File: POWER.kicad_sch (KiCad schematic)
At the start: 15 parts, among them U1 XL1509-5.0, U3 SY8089AAC

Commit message: 更新原理图
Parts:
- added C39: 1nF, symbol Device:C_Small
- added D4: SMBJ24A, kicad_api_lib:SMBJ24A, symbol SMBJ24A:D_Schottky_Filled
- added R10: 1M, symbol Device:R_US
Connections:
- net GND: now also C39.1, R10.1
- net VIN: no longer names the net of C2.1, U1.1 (VIN)
- net VIN: now also D4.1 (K)
- new net +24V: D4.2 (A)
- new net Earth: C39.2, R10.2

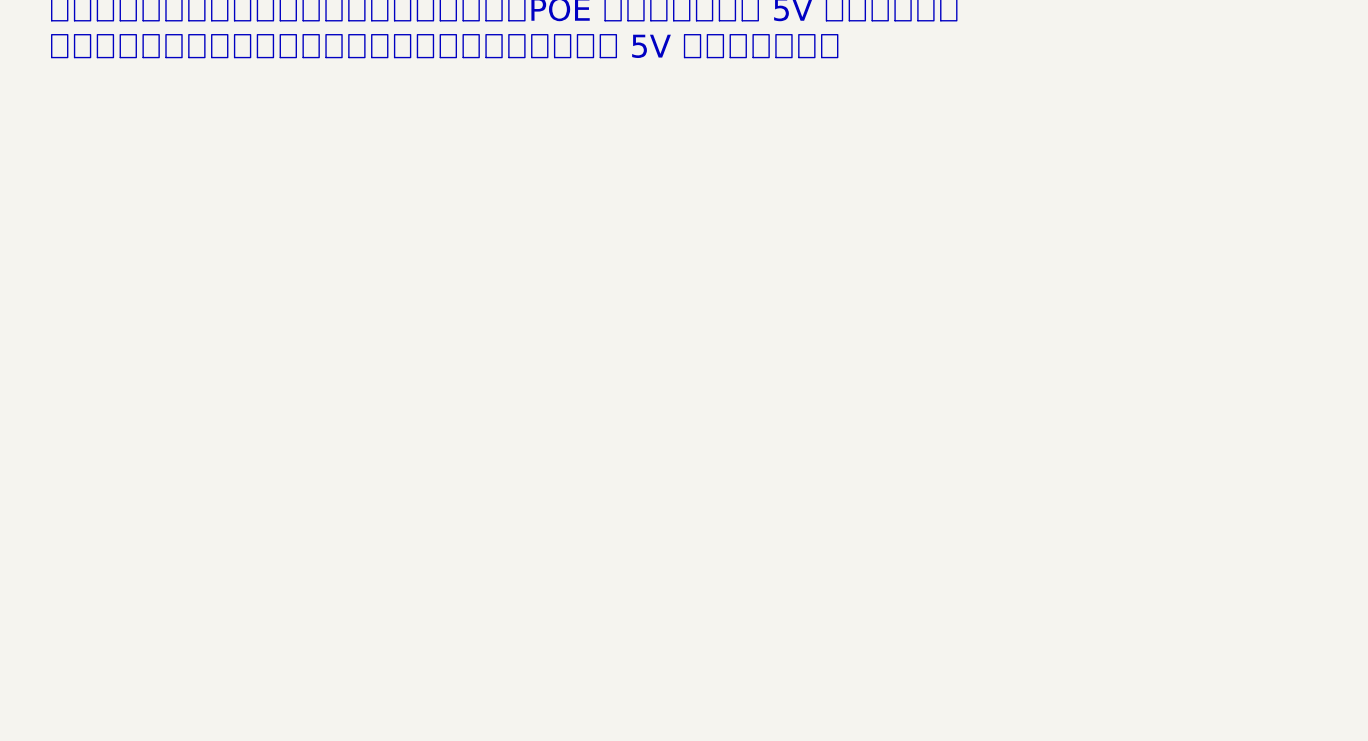
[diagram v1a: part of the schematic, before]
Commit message: 增加USB,TYPEC转串口esd隔离，
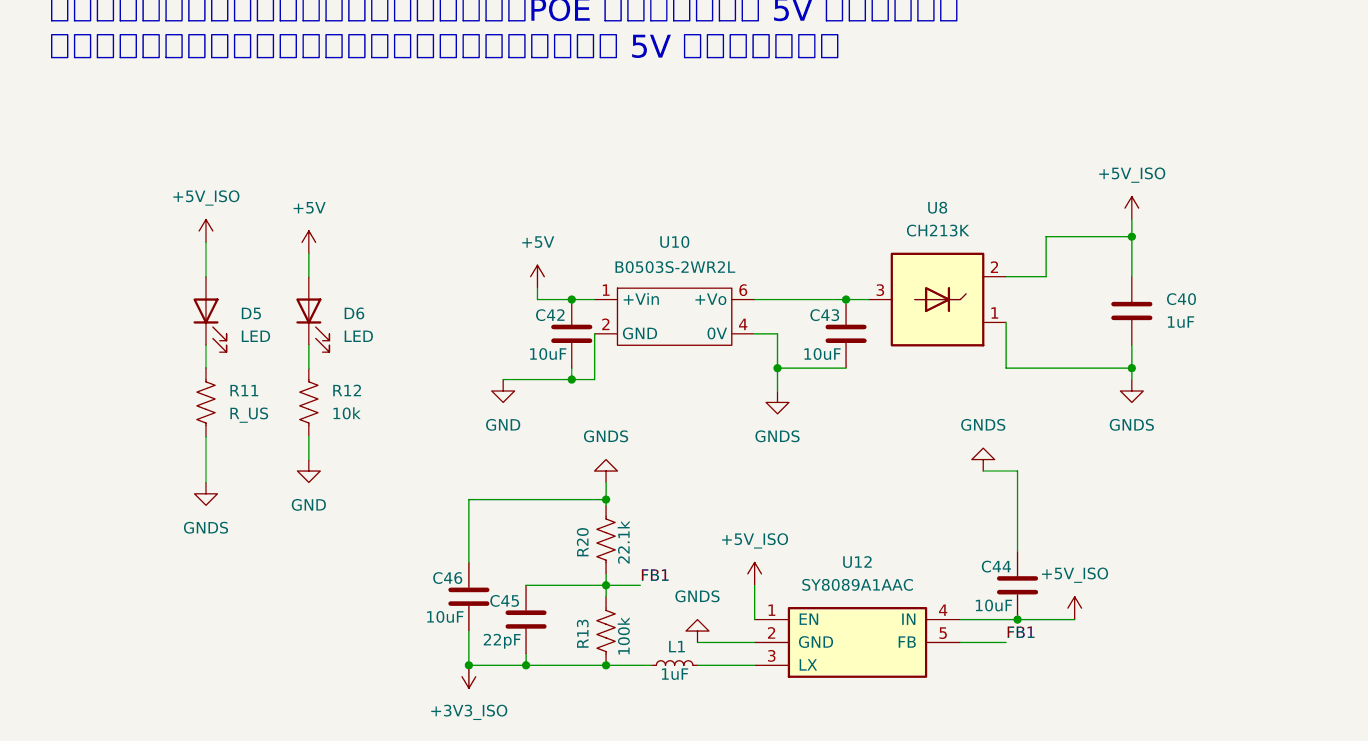
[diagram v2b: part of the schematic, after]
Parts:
- added C40: 1uF, symbol Device:C
- added C42, C43, C44, C46: 10uF, symbol Device:C
- added C45: 22pF, symbol Device:C
- added D5, D6: LED, symbol Device:LED
- added L1: 1uF, symbol Device:L_Small
- added R11: R_US, symbol Device:R_US
- added R12: 10k, symbol Device:R_US
- added R13: 100k, symbol Device:R_US
- added R20: 22.1k, symbol Device:R_US
- added U10: B0503S-2WR2L, Package_SIP:SIP4_Sharp-SSR_P7.62mm_Straight, symbol B0503S-2WL:B0503S-2WL
- added U12: SY8089A1AAC, kicad_api_lib:SY8089A1AAC, symbol SY8089A1AAC:SYH407AAC
- added U8: CH213K, kicad_api_lib:CH213K, symbol CH213K:WCH_CH213K
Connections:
- net +5V: now also C42.1, D6.2 (A), U10.1 (+Vin)
- net GND: now also C42.2, R12.2, U10.2 (GND)
- new net: C43.1, U10.6 (+Vo), U8.3 (VI+)
- new net: L1.2, U12.3 (LX)
- new net: D5.1 (K), R11.1
- new net: D6.1 (K), R12.1
- new net +3V3_ISO: C45.2, C46.2, L1.1, R13.2
- new net +5V_ISO: C40.1, C44.2, D5.2 (A), U12.1 (EN), U12.4 (IN), U8.2 (VO-)
- new net FB1: C45.1, R13.1, R20.2, U12.5 (FB)
- new net GNDS: C40.2, C43.2, C44.1, C46.1, R11.2, R20.1, U10.4 (0V), U12.2 (GND), U8.1 (GND)

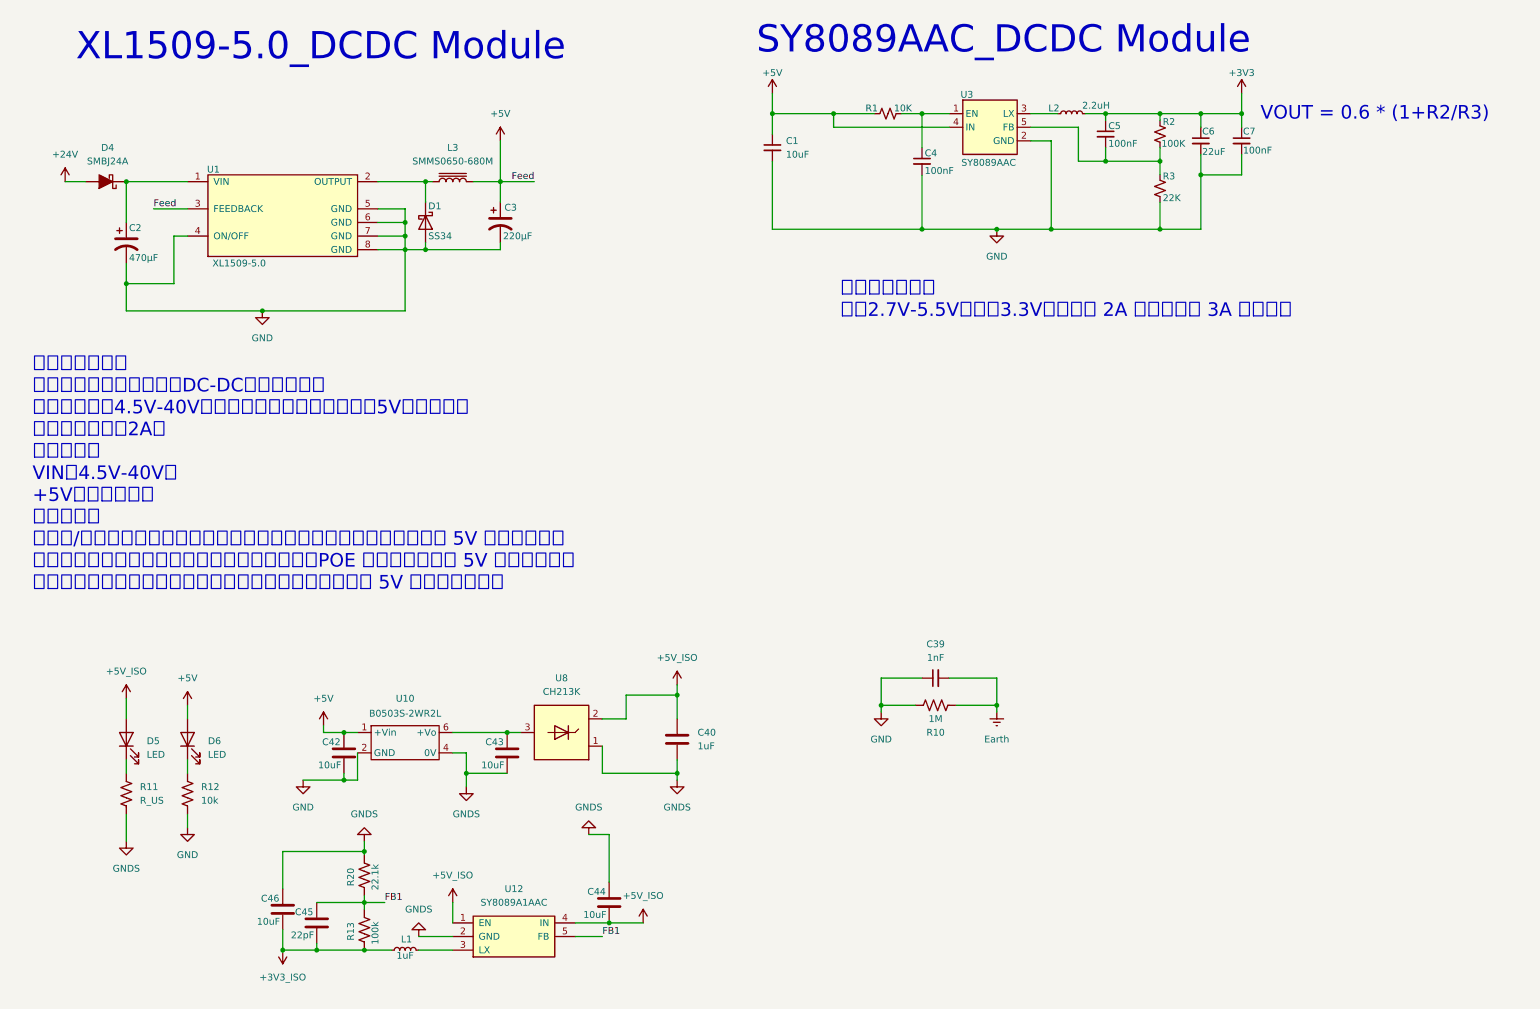
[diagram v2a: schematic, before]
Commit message: 完成GD32F303控制板原理图与PCB设计
- 更新电源、CAN、RS232、RS485及电机通信子电路
- 切换并完善GD32F303VCT6核心原理图
- 新增PCB布局及所需符号、封装库文件
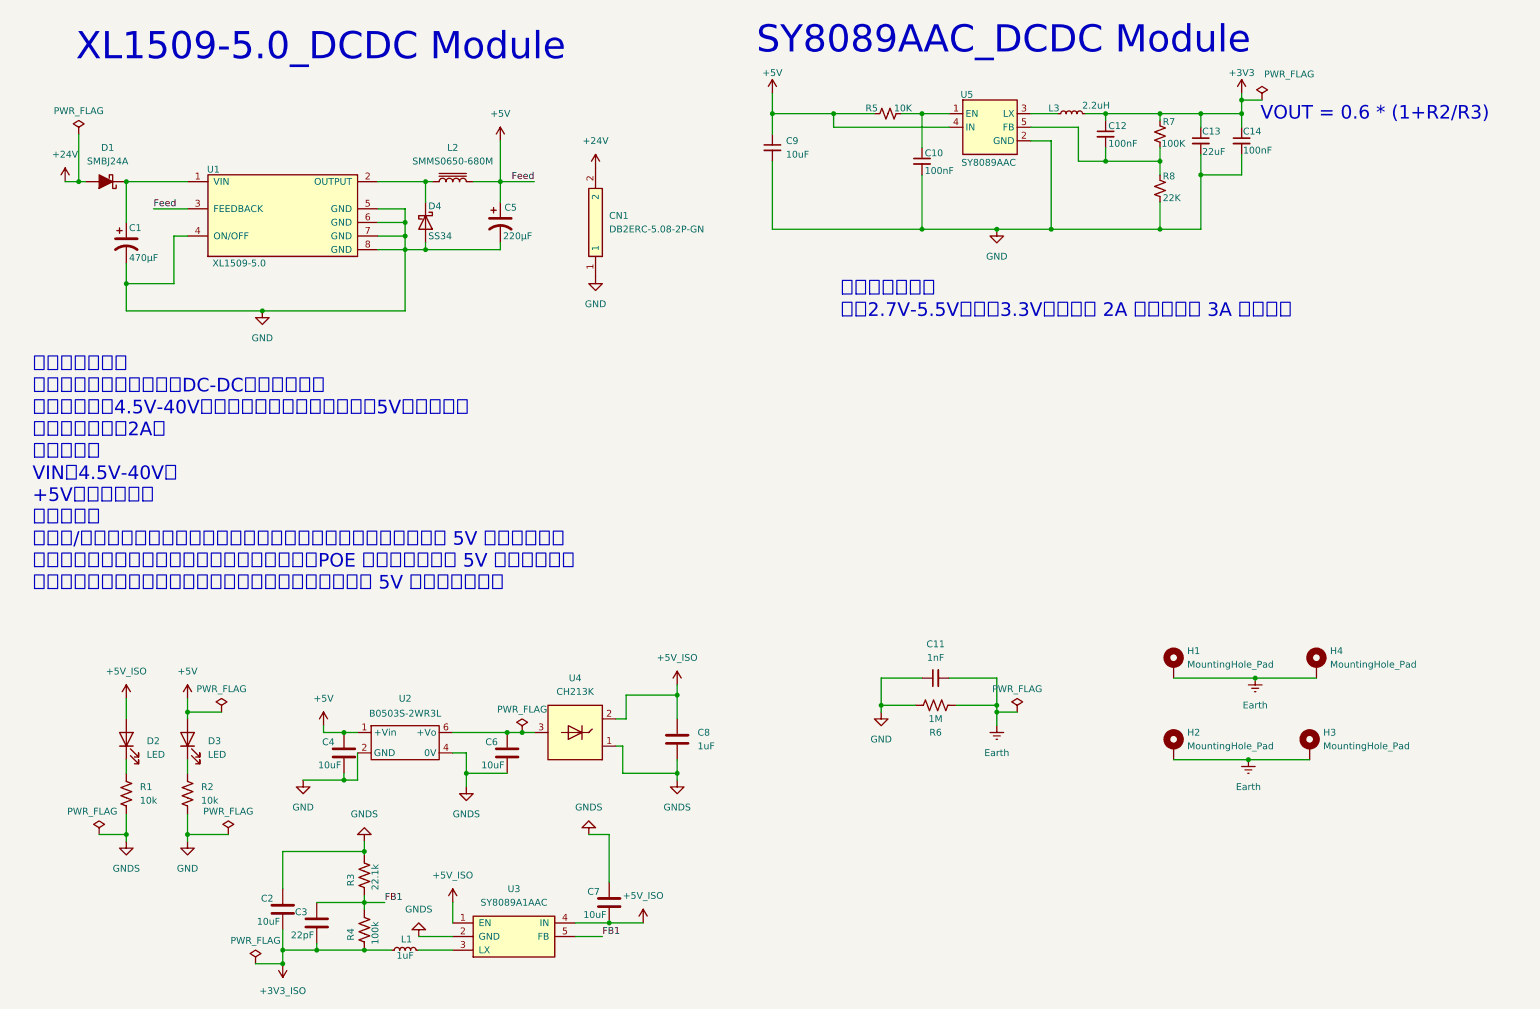
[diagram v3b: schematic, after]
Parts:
- added CN1: DB2ERC-5.08-2P-GN, kicad_api_lib:DB2ERC-5.08-2P-GN, symbol DB2ERC-5.08-2P-GN:KF237-10.16-2P
- added H1, H2, H3, H4: MountingHole_Pad, MountingHole:MountingHole_3.2mm_M3_ISO7380_Pad, symbol Mechanical:MountingHole_Pad
- C1: renamed from C2; footprint kicad_api_lib:RVT1E471M0810 -> Capacitor_SMD:CP_Elec_10x10.5
- C10: renamed from C4; footprint kicad_api_lib:0402B104K500CT -> Capacitor_SMD:C_0603_1608Metric_Pad1.08x0.95mm_HandSolder
- C11: renamed from C39; footprint (none) -> Capacitor_SMD:C_0603_1608Metric_Pad1.08x0.95mm_HandSolder
- C12: renamed from C5; footprint kicad_api_lib:0402B104K500CT -> Capacitor_SMD:C_0402_1005Metric_Pad0.74x0.62mm_HandSolder
- C13: renamed from C6; footprint kicad_api_lib:GRM188R61A226ME15D -> Capacitor_SMD:C_0603_1608Metric_Pad1.08x0.95mm_HandSolder
- C14: renamed from C7; footprint kicad_api_lib:0402B104K500CT -> Capacitor_SMD:C_0402_1005Metric_Pad0.74x0.62mm_HandSolder
- C2: renamed from C46; footprint (none) -> Capacitor_SMD:C_0603_1608Metric_Pad1.08x0.95mm_HandSolder
- C3: renamed from C45; footprint (none) -> Capacitor_SMD:C_0603_1608Metric_Pad1.08x0.95mm_HandSolder
- C4: renamed from C42; footprint (none) -> Capacitor_SMD:C_0603_1608Metric_Pad1.08x0.95mm_HandSolder
- C5: renamed from C3; footprint kicad_api_lib:RVT1E221M0607 -> Capacitor_SMD:CP_Elec_5x5.4
- C6: renamed from C43; footprint (none) -> Capacitor_SMD:C_0603_1608Metric_Pad1.08x0.95mm_HandSolder
- C7: renamed from C44; footprint (none) -> Capacitor_SMD:C_0805_2012Metric_Pad1.18x1.45mm_HandSolder
- C8: renamed from C40; footprint (none) -> Capacitor_SMD:C_0603_1608Metric_Pad1.08x0.95mm_HandSolder
- C9: renamed from C1; footprint kicad_api_lib:CL10A106MP8NNNC -> Capacitor_SMD:C_0603_1608Metric_Pad1.08x0.95mm_HandSolder
- D2: renamed from D5; footprint (none) -> LED_SMD:LED_0603_1608Metric_Pad1.05x0.95mm_HandSolder
- D3: renamed from D6; footprint (none) -> LED_SMD:LED_0603_1608Metric_Pad1.05x0.95mm_HandSolder
- D4: renamed from D1; footprint kicad_api_lib:SS34 -> Diode_SMD:D_SMA
- L1: footprint (none) -> Capacitor_SMD:C_0603_1608Metric_Pad1.08x0.95mm_HandSolder
- L3: renamed from L2; footprint kicad_api_lib:SWPA3015S2R2NT -> Inductor_SMD_Wurth:L_Wurth_WE-LQSH-3012
- R1: renamed from R11; value R_US -> 10k; footprint (none) -> Resistor_SMD:R_0603_1608Metric_Pad0.98x0.95mm_HandSolder
- R2: renamed from R12; footprint (none) -> Resistor_SMD:R_0603_1608Metric_Pad0.98x0.95mm_HandSolder
- R3: renamed from R20; footprint (none) -> Resistor_SMD:R_0603_1608Metric_Pad0.98x0.95mm_HandSolder
- R4: renamed from R13; footprint (none) -> Resistor_SMD:R_0603_1608Metric_Pad0.98x0.95mm_HandSolder
- R5: renamed from R1; footprint kicad_api_lib:RC0402JR-0710KL -> Resistor_SMD:R_0402_1005Metric_Pad0.72x0.64mm_HandSolder
- R6: renamed from R10; footprint (none) -> Resistor_SMD:R_0603_1608Metric_Pad0.98x0.95mm_HandSolder
- R7: renamed from R2; footprint kicad_api_lib:WR04X1003FTL -> Resistor_SMD:R_01005_0402Metric_Pad0.57x0.30mm_HandSolder
- R8: renamed from R3; footprint kicad_api_lib:CRCW040222K0FKED -> Resistor_SMD:R_01005_0402Metric_Pad0.57x0.30mm_HandSolder
- U1: footprint kicad_api_lib:XL1509-5.0 -> Package_SO:SOIC-8_3.9x4.9mm_P1.27mm
- U2: renamed from U10; value B0503S-2WR2L -> B0503S-2WR3L; footprint Package_SIP:SIP4_Sharp-SSR_P7.62mm_Straight -> Converter_DCDC:B0503S-2WR3L
- U5: renamed from U3; footprint kicad_api_lib:SY8089AAC -> Package_TO_SOT_SMD:SOT-23-5_HandSoldering
- renumbered D4 to D1, L3 to L2, U12 to U3, U8 to U4
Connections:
- net +24V: now also CN1.2
- net Earth: now also H1.1, H2.1, H3.1, H4.1
- net GND: now also CN1.1
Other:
- moved on the sheet: U4

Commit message: 优化接口原理图与PCB布局
- 精简CAN接口并调整各子页器件编号
- 更新电源输入端子与Type-C接口封装
- 重新整理控制板PCB器件布局
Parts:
- removed CN1: DB2ERC-5.08-2P-GN, kicad_api_lib:DB2ERC-5.08-2P-GN, symbol DB2ERC-5.08-2P-GN:KF237-10.16-2P
- added CN1: KF128L-5.08-2P, kicad_api_lib:KF128L-5.08-2P, symbol KF128L-5.08-2P:15ETYRC-3.5-02P-14-00AH
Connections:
- net +24V: now also CN1.2
- net GND: now also CN1.1
